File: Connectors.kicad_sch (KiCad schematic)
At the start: 4 parts, among them J1 Conn_01x04_Pin, J2 Conn_01x09_Pin, J3 Conn_01x04_Pin, J4 Conn_02x03_Odd_Even

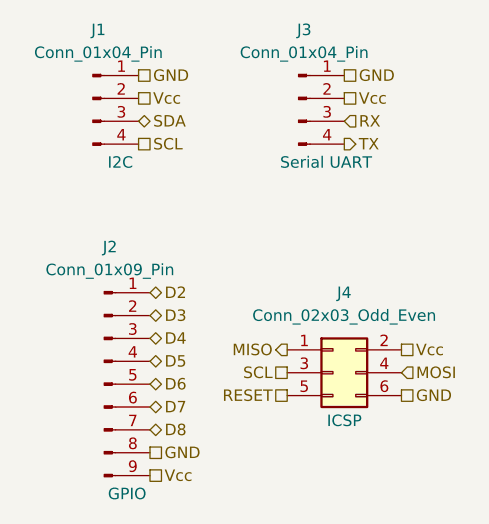
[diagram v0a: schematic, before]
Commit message: Routing, GND Plane, Rework VCC Line and slick Screen complete
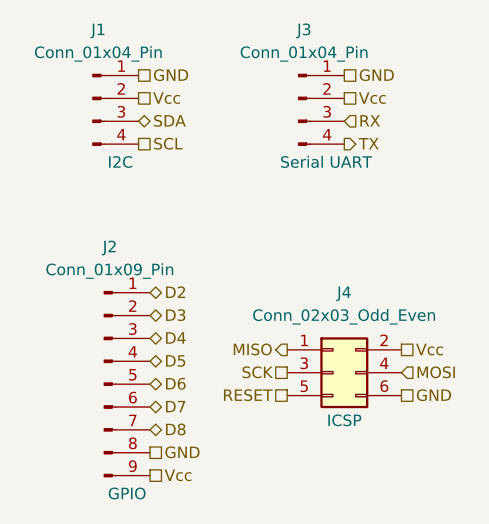
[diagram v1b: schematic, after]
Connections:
- net SCL: no longer J4.3 (Pin_3)
- new net SCK: J4.3 (Pin_3)
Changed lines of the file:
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@@
 	(generator_version "9.0")
 	(paper "A4")
-	(hierarchical_label "SCL"
+	(hierarchical_label "SCK"
 		(shape passive)
 		(at 133.35 115.57 180)
